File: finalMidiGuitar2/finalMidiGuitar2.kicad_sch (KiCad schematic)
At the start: 17 parts, among them J1 PinHeader_01x06_P2.54mm_Verti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, J3 NeoPixel, J4 Oled Display, M1 Module_XIAO_Generic_SocketSMD, SW1 BTN, U1 LevelShifter

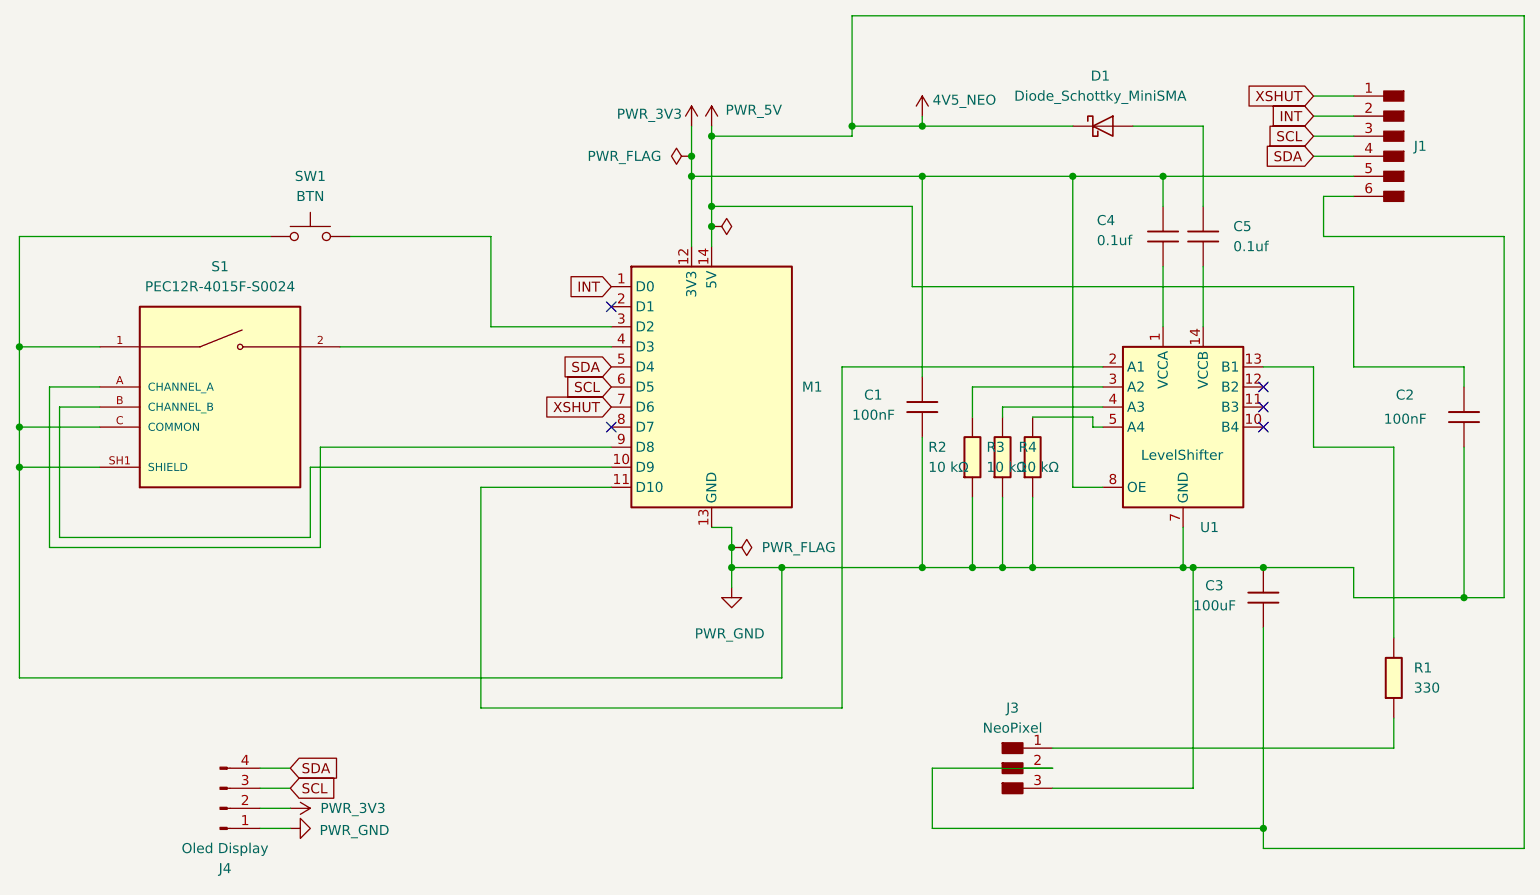
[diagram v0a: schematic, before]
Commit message: Remove lock files for KiCad PCB and schematic
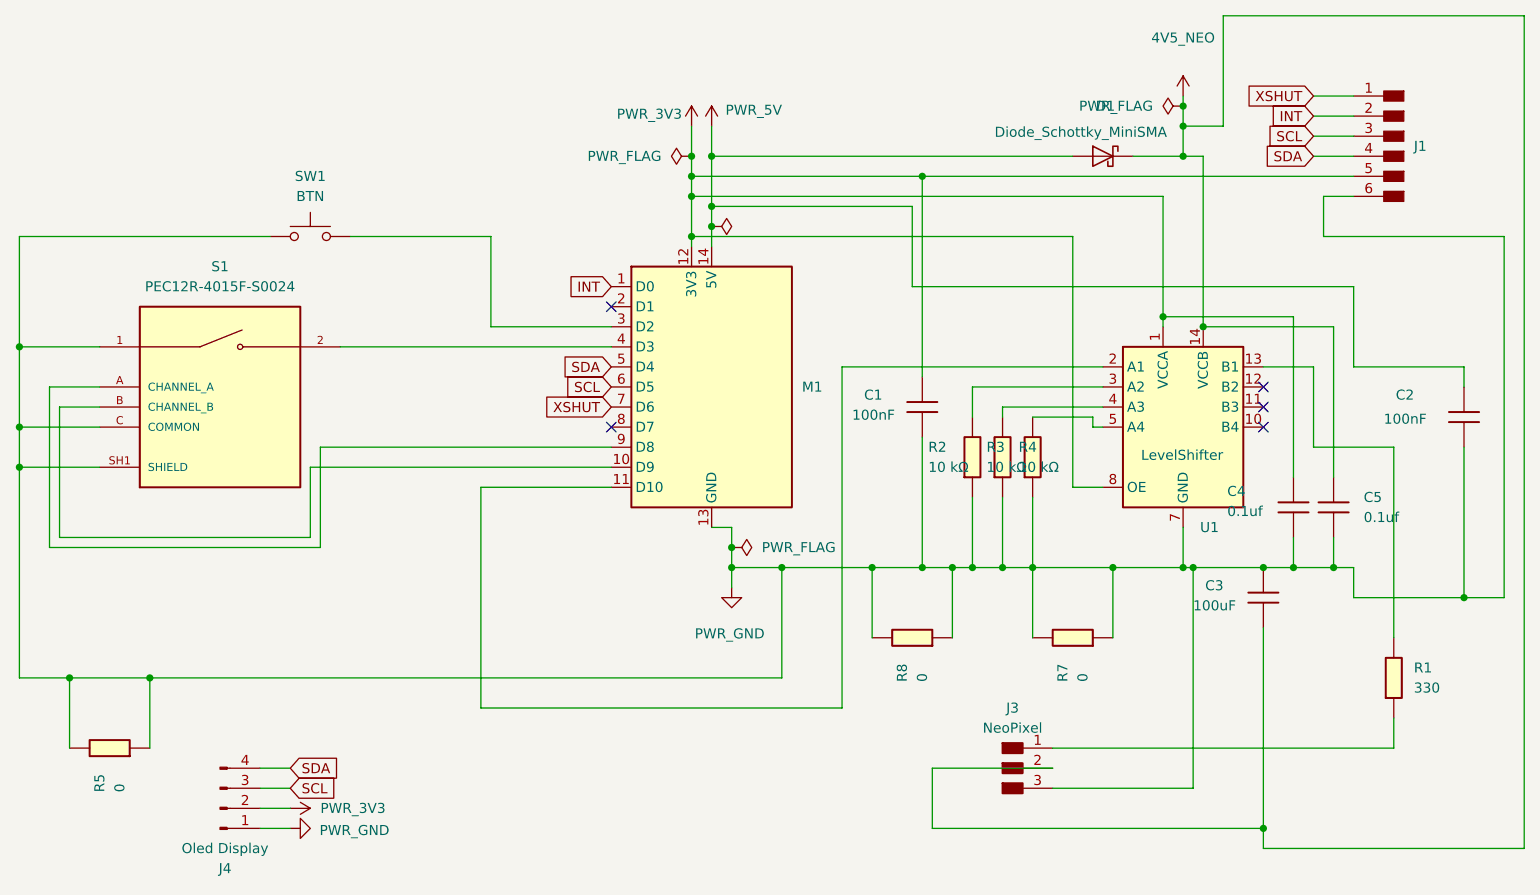
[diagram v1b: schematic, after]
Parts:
- added R5, R7, R8: 0, PCM_fab:R_1206, symbol PCM_fab:R_1206
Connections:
- net 4V5_NEO: now also C5.1, U1.14 (VCCB); no longer C2.1, M1.14 (5V)
- net PWR_3V3: now also U1.1 (VCCA)
- net PWR_GND: now also C4.2, C5.2, R5.1, R5.2, R7.1, R7.2, R8.1, R8.2
- net PWR_5V: now reaches D1.2 (A)
- net PWR_5V: now also C2.1, M1.14 (5V); no longer C5.1
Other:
- moved on the sheet: C4, C5, D1
